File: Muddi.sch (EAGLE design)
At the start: 12 parts, among them IC1 7805TV, J1 DCJ0202

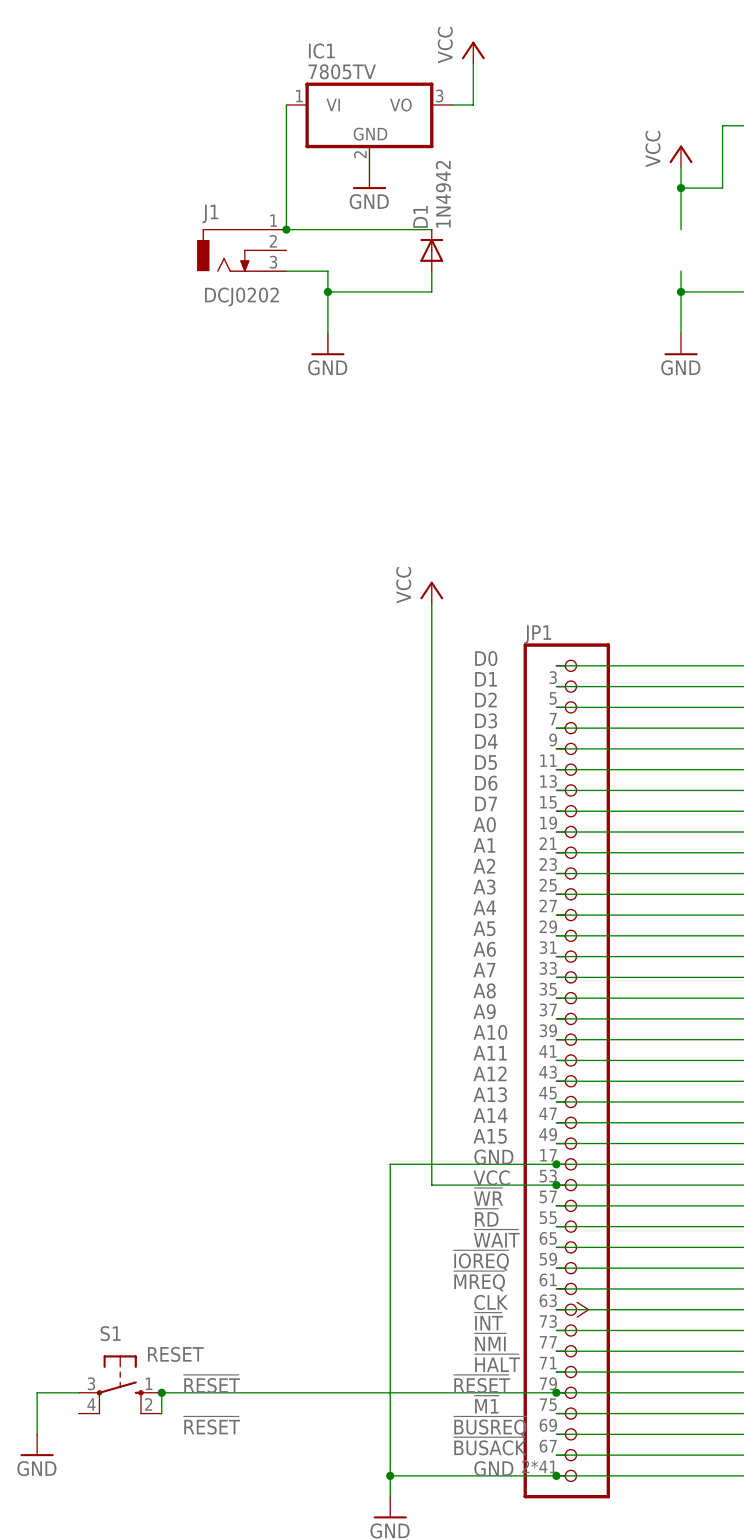
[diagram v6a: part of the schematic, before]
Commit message: Use MAX811 for Reset. Add Power Capacitors.
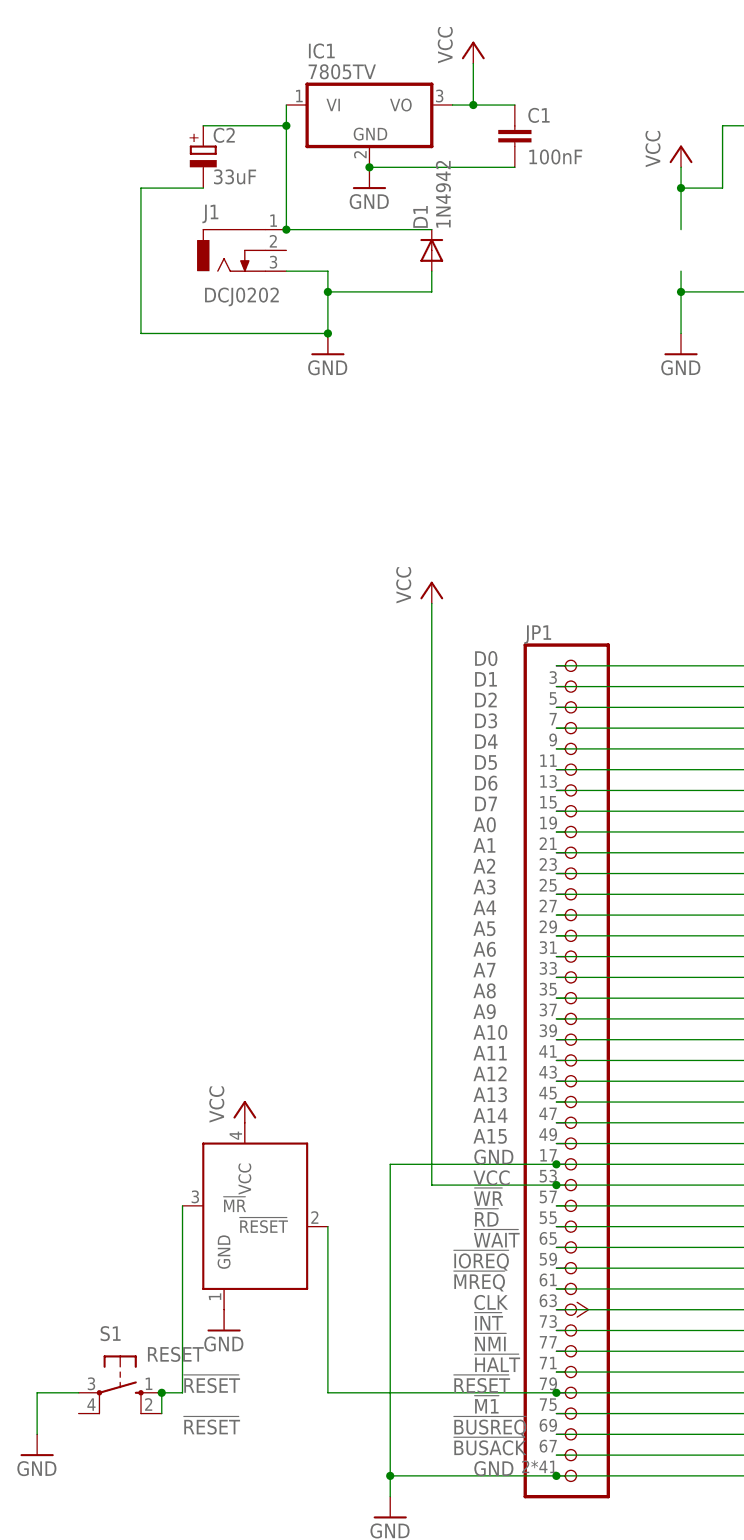
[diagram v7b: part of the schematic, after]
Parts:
- added C1: 100nF, capacitor-wima:C2.5/2
- added C2: 33uF, rcl:CPOL-EUE2.5-7
- added MAX811: MAX811, jean:MAX811
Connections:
- new net N$27: MAX811.!MR, S1.S, S1.S1
- net GND: now also C1.2, C2.-, MAX811.GND
- net N$26: now also C2.+
- net N$40: now also MAX811.!RESET; no longer S1.S, S1.S1
- net VCC: now also C1.1, MAX811.VCC
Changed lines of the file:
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@@
 <part name="GND1" library="supply1" deviceset="GND" device=""/>
 <part name="GND3" library="supply1" deviceset="GND" device=""/>
+<part name="MAX811" library="jean" deviceset="MAX811" device=""/>
+<part name="GND4" library="supply1" deviceset="GND" device=""/>
+<part name="P+3" library="supply1" deviceset="VCC" device=""/>
+<part name="C1" library="capacitor-wima" deviceset="C" device="2.5/2" value="100nF"/>
+<part name="C2" library="rcl" deviceset="CPOL-EU" device="E2.5-7" value="33uF"/>
 </parts>
 <sheets>
@@
 <instance part="GND1" gate="1" x="-25.4" y="261.62"/>
 <instance part="GND3" gate="1" x="-30.48" y="241.3"/>
+<instance part="MAX811" gate="G$1" x="-38.1" y="134.62"/>
+<instance part="GND4" gate="1" x="-43.18" y="121.92"/>
+<instance part="P+3" gate="VCC" x="-40.64" y="149.86"/>
+<instance part="C1" gate="G$1" x="-7.62" y="269.24"/>
+<instance part="C2" gate="G$1" x="-45.72" y="266.7"/>
 </instances>
 <busses>
@@
 <wire x1="172.72" y1="114.3" x2="134.62" y2="114.3" width="0.1524" layer="91"/>
 <junction x="134.62" y="114.3"/>
-<pinref part="S1" gate="1" pin="S"/>
-<wire x1="-2.54" y1="114.3" x2="-50.8" y2="114.3" width="0.1524" layer="91"/>
+<pinref part="MAX811" gate="G$1" pin="!RESET"/>
+<wire x1="-2.54" y1="114.3" x2="-30.48" y2="114.3" width="0.1524" layer="91"/>
+<wire x1="-30.48" y1="114.3" x2="-30.48" y2="134.62" width="0.1524" layer="91"/>
 <junction x="-2.54" y="114.3"/>
-<pinref part="S1" gate="1" pin="S1"/>
-<wire x1="-50.8" y1="114.3" x2="-50.8" y2="111.76" width="0.1524" layer="91"/>
-<junction x="-50.8" y="114.3"/>
 </segment>
 </net>
@@
 <wire x1="-15.24" y1="271.78" x2="-12.7" y2="271.78" width="0.1524" layer="91"/>
 <wire x1="-12.7" y1="271.78" x2="-12.7" y2="276.86" width="0.1524" layer="91"/>
+<pinref part="C1" gate="G$1" pin="1"/>
+<wire x1="-12.7" y1="271.78" x2="-7.62" y2="271.78" width="0.1524" layer="91"/>
+<junction x="-12.7" y="271.78"/>
+</segment>
+<segment>
+<pinref part="MAX811" gate="G$1" pin="VCC"/>
+<pinref part="P+3" gate="VCC" pin="VCC"/>
 </segment>
 </net>
@@
 <pinref part="IC1" gate="A1" pin="GND"/>
 <pinref part="GND1" gate="1" pin="GND"/>
+<pinref part="C1" gate="G$1" pin="2"/>
+<wire x1="-7.62" y1="264.16" x2="-25.4" y2="264.16" width="0.1524" layer="91"/>
+<junction x="-25.4" y="264.16"/>
 </segment>
 <segment>
@@
 <wire x1="-30.48" y1="248.92" x2="-17.78" y2="248.92" width="0.1524" layer="91"/>
 <junction x="-30.48" y="248.92"/>
+<pinref part="C2" gate="G$1" pin="-"/>
+<wire x1="-45.72" y1="261.62" x2="-53.34" y2="261.62" width="0.1524" layer="91"/>
+<wire x1="-53.34" y1="261.62" x2="-53.34" y2="243.84" width="0.1524" layer="91"/>
+<wire x1="-53.34" y1="243.84" x2="-30.48" y2="243.84" width="0.1524" layer="91"/>
+<junction x="-30.48" y="243.84"/>
+</segment>
+<segment>
+<pinref part="MAX811" gate="G$1" pin="GND"/>
+<pinref part="GND4" gate="1" pin="GND"/>
 </segment>
 </net>
@@
 <pinref part="J1" gate="G$1" pin="1"/>
 <pinref part="IC1" gate="A1" pin="VI"/>
-<wire x1="-35.56" y1="256.54" x2="-35.56" y2="271.78" width="0.1524" layer="91"/>
+<wire x1="-35.56" y1="256.54" x2="-35.56" y2="269.24" width="0.1524" layer="91"/>
 <pinref part="D1" gate="1" pin="C"/>
+<wire x1="-35.56" y1="269.24" x2="-35.56" y2="271.78" width="0.1524" layer="91"/>
 <wire x1="-17.78" y1="256.54" x2="-35.56" y2="256.54" width="0.1524" layer="91"/>
 <junction x="-35.56" y="256.54"/>
-</segment>
-</net>
+<pinref part="C2" gate="G$1" pin="+"/>
+<wire x1="-45.72" y1="269.24" x2="-35.56" y2="269.24" width="0.1524" layer="91"/>
+<junction x="-35.56" y="269.24"/>
+</segment>
+</net>
+<net name="N$27" class="0">
+<segment>
+<pinref part="S1" gate="1" pin="S1"/>
+<pinref part="S1" gate="1" pin="S"/>
+<wire x1="-50.8" y1="114.3" x2="-50.8" y2="111.76" width="0.1524" layer="91"/>
+<pinref part="MAX811" gate="G$1" pin="!MR"/>
+<wire x1="-50.8" y1="114.3" x2="-48.26" y2="114.3" width="0.1524" layer="91"/>
+<wire x1="-48.26" y1="114.3" x2="-48.26" y2="137.16" width="0.1524" layer="91"/>
+<junction x="-50.8" y="114.3"/>
+</segment>
+</net>

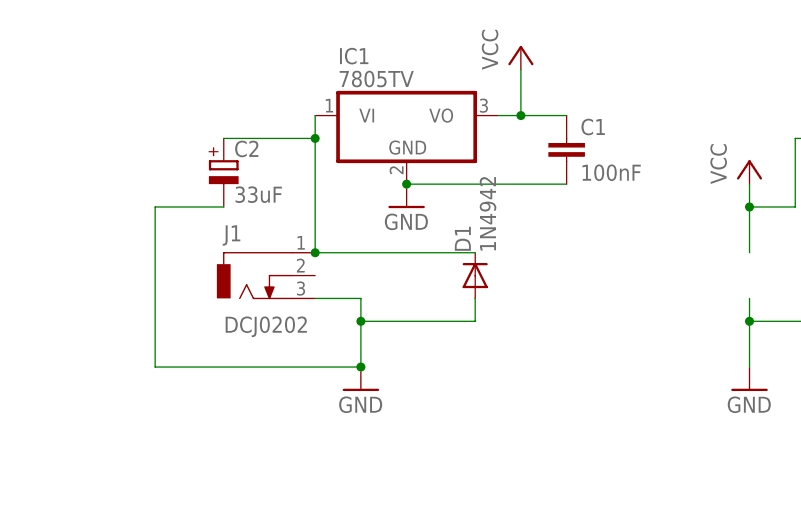
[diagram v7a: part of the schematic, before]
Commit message: Fix incorrectly connected diode
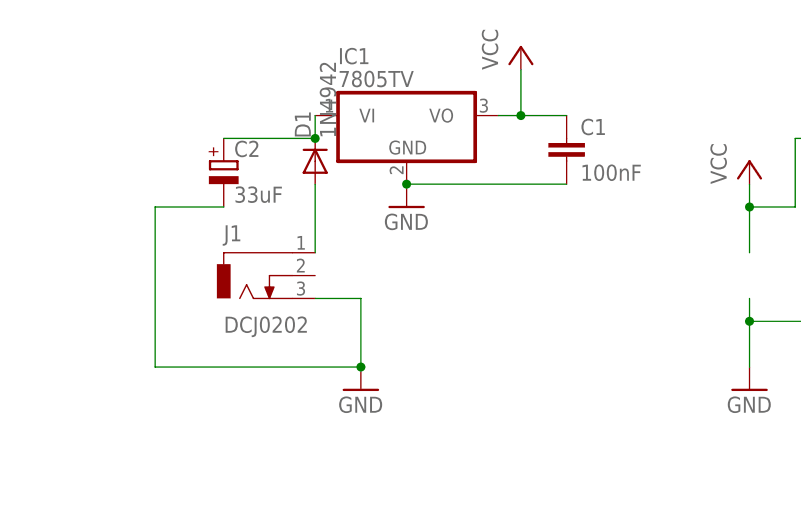
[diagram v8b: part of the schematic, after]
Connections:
- new net N$28: D1.A, J1.1
- net GND: no longer D1.A
- net N$26: no longer J1.1
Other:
- moved on the sheet: D1
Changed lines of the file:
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@@
 <instance part="GND" gate="1" x="12.7" y="241.3"/>
 <instance part="VCC" gate="VCC" x="12.7" y="266.7"/>
-<instance part="D1" gate="1" x="-17.78" y="254" rot="R90">
-<attribute name="OC_FARNELL" x="-17.78" y="254" size="1.778" layer="96" display="off"/>
-<attribute name="MF" x="-17.78" y="254" size="1.778" layer="96" display="off"/>
-<attribute name="MPN" x="-17.78" y="254" size="1.778" layer="96" display="off"/>
+<instance part="D1" gate="1" x="-35.56" y="266.7" rot="R90">
+<attribute name="OC_FARNELL" x="-35.56" y="266.7" size="1.778" layer="96" display="off"/>
+<attribute name="MF" x="-35.56" y="266.7" size="1.778" layer="96" display="off"/>
+<attribute name="MPN" x="-35.56" y="266.7" size="1.778" layer="96" display="off"/>
 </instance>
 <instance part="P+2" gate="VCC" x="-17.78" y="213.36"/>
@@
 <pinref part="GND3" gate="1" pin="GND"/>
 <wire x1="-35.56" y1="251.46" x2="-30.48" y2="251.46" width="0.1524" layer="91"/>
-<wire x1="-30.48" y1="251.46" x2="-30.48" y2="248.92" width="0.1524" layer="91"/>
-<pinref part="D1" gate="1" pin="A"/>
-<wire x1="-30.48" y1="248.92" x2="-30.48" y2="243.84" width="0.1524" layer="91"/>
-<wire x1="-17.78" y1="251.46" x2="-17.78" y2="248.92" width="0.1524" layer="91"/>
-<wire x1="-30.48" y1="248.92" x2="-17.78" y2="248.92" width="0.1524" layer="91"/>
-<junction x="-30.48" y="248.92"/>
+<wire x1="-30.48" y1="251.46" x2="-30.48" y2="243.84" width="0.1524" layer="91"/>
 <pinref part="C2" gate="G$1" pin="-"/>
 <wire x1="-45.72" y1="261.62" x2="-53.34" y2="261.62" width="0.1524" layer="91"/>
@@
 <net name="N$26" class="0">
 <segment>
-<pinref part="J1" gate="G$1" pin="1"/>
 <pinref part="IC1" gate="A1" pin="VI"/>
-<wire x1="-35.56" y1="256.54" x2="-35.56" y2="269.24" width="0.1524" layer="91"/>
-<pinref part="D1" gate="1" pin="C"/>
 <wire x1="-35.56" y1="269.24" x2="-35.56" y2="271.78" width="0.1524" layer="91"/>
-<wire x1="-17.78" y1="256.54" x2="-35.56" y2="256.54" width="0.1524" layer="91"/>
-<junction x="-35.56" y="256.54"/>
 <pinref part="C2" gate="G$1" pin="+"/>
 <wire x1="-45.72" y1="269.24" x2="-35.56" y2="269.24" width="0.1524" layer="91"/>
+<pinref part="D1" gate="1" pin="C"/>
 <junction x="-35.56" y="269.24"/>
 </segment>
@@
 </segment>
 </net>
+<net name="N$28" class="0">
+<segment>
+<pinref part="J1" gate="G$1" pin="1"/>
+<pinref part="D1" gate="1" pin="A"/>
+<wire x1="-35.56" y1="256.54" x2="-35.56" y2="264.16" width="0.1524" layer="91"/>
+</segment>
+</net>
